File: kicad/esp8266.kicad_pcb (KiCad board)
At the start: 2 copper layers, 100 x 100 mm, 43 parts, among them J1 BATT, J2 Conn_Coaxial_Power, J3 CONN FT232RL, J4 RJ12, J5 RJ12, J6 Onewire, J7 Onewire, J8 Conn_01x01_Male, Q1 BSP75, Q2 BSP75, Q3 BSP75, Q4 BSP75, SW1 RESET, SW2 PROG, U1 ESP-12E, U2 MCP73831-2, U3 MCP1703A-3302_SOT23, U4 MS5637, U5 MCP1703A-5002_SOT23, U6 Si7020-A20, U7 DS18B20

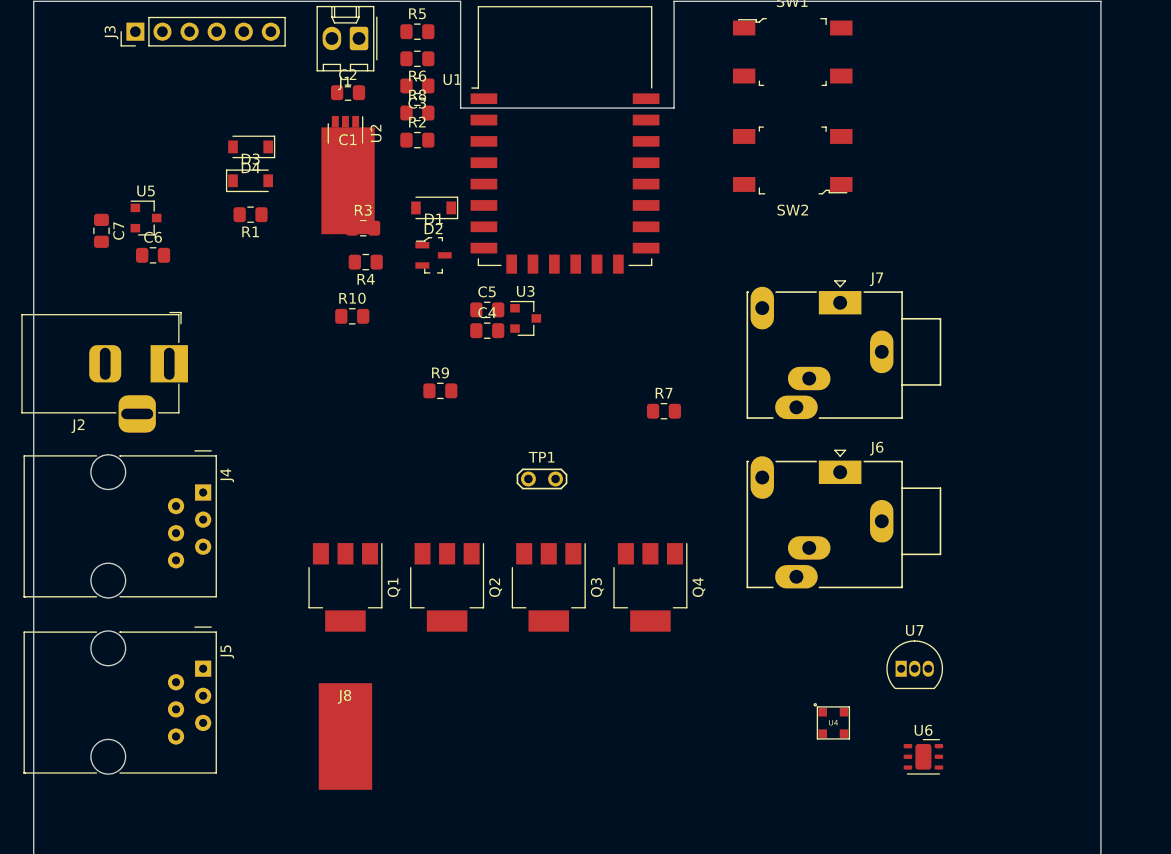
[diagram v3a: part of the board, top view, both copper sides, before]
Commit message: add test points in kicad
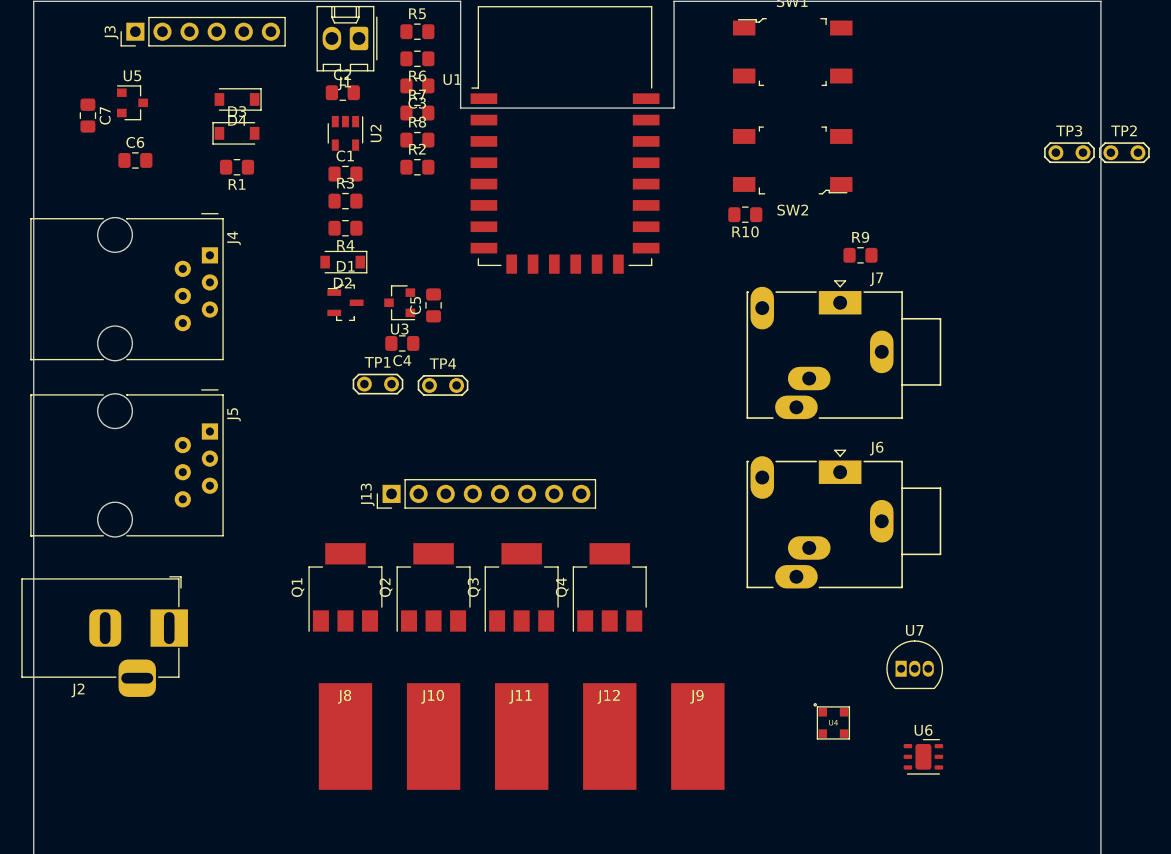
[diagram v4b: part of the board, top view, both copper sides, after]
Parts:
- added J10: Green, Connector_Wire:SolderWirePad_1x01_SMD_5x10mm, F.Cu at (115.5, 130.9)
- added J11: Blue, Connector_Wire:SolderWirePad_1x01_SMD_5x10mm, F.Cu at (123.7, 130.9)
- added J12: White, Connector_Wire:SolderWirePad_1x01_SMD_5x10mm, F.Cu at (132.0, 130.9)
- added J13: Conn_01x08_Female, Connector_PinHeader_2.54mm:PinHeader_1x08_P2.54mm_Vertical, F.Cu at (111.5, 108.2)
- added J9: Pad, Connector_Wire:SolderWirePad_1x01_SMD_5x10mm, F.Cu at (140.2, 130.9)
- added TP2: TestPoint_2Pole, TestPoint:TestPoint_2Pads_Pitch2.54mm_Drill0.8mm, F.Cu at (178.9, 76.2)
- added TP3: TestPoint_2Pole, TestPoint:TestPoint_2Pads_Pitch2.54mm_Drill0.8mm, F.Cu at (173.8, 76.2)
- added TP4: TestPoint_2Pole, TestPoint:TestPoint_2Pads_Pitch2.54mm_Drill0.8mm, F.Cu at (115.1, 98.0)
- C1: footprint Connector_Wire:SolderWirePad_1x01_SMD_5x10mm -> Capacitor_SMD:C_0805_2012Metric_Pad1.15x1.40mm_HandSolder
- J8: value Conn_01x01_Male -> Red
- moved R9 41.4 mm to (155.5, 85.8)
- moved R10 38.0 mm to (144.7, 82.0), turned to 180 degrees
- moved R7 36.3 mm to (114.0, 72.5)
- moved J2 24.8 mm to (90.7, 120.7)
- moved J4 22.2 mm to (94.5, 85.8)
- moved J5 22.2 mm to (94.5, 102.3)
- moved TP1 17.8 mm to (109.0, 97.9)
- moved U3 11.9 mm to (112.3, 90.2), turned to 180 degrees
- moved C7 10.9 mm to (83.1, 72.7)
- moved U5 10.9 mm to (87.3, 71.5)
- moved D2 9.91 mm to (107.0, 86.4)
- moved D1 9.38 mm to (107.2, 90.2)
- moved C6 9.04 mm to (87.5, 76.9)
- moved C4 8.05 mm to (112.5, 94.1), turned to 180 degrees
- moved C5 5.05 mm to (115.5, 90.5), turned to 90 degrees
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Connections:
- net /VBAT renamed +BATT
- Q2 pad 1: Net-(Q2-Pad1) -> /IO13
- Q2 pad 3: Net-(Q2-Pad3) -> GND
- Q3 pad 1: Net-(Q3-Pad1) -> /IO14
- Q3 pad 3: Net-(Q3-Pad3) -> GND
- Q4 pad 1: Net-(Q4-Pad1) -> /IO15
- Q4 pad 3: Net-(Q4-Pad3) -> GND
- U4 pad 1: Net-(U4-Pad1) -> +3V3
- U4 pad 2: Net-(U4-Pad2) -> /SDA
- U4 pad 3: Net-(U4-Pad3) -> /SCL
- U4 pad 4: Net-(U4-Pad4) -> GND
- U6 pad 1: Net-(U6-Pad1) -> /SDA
- U6 pad 2: Net-(U6-Pad2) -> GND
- U6 pad 5: Net-(U6-Pad5) -> +3V3
- U6 pad 6: Net-(U6-Pad6) -> /SCL

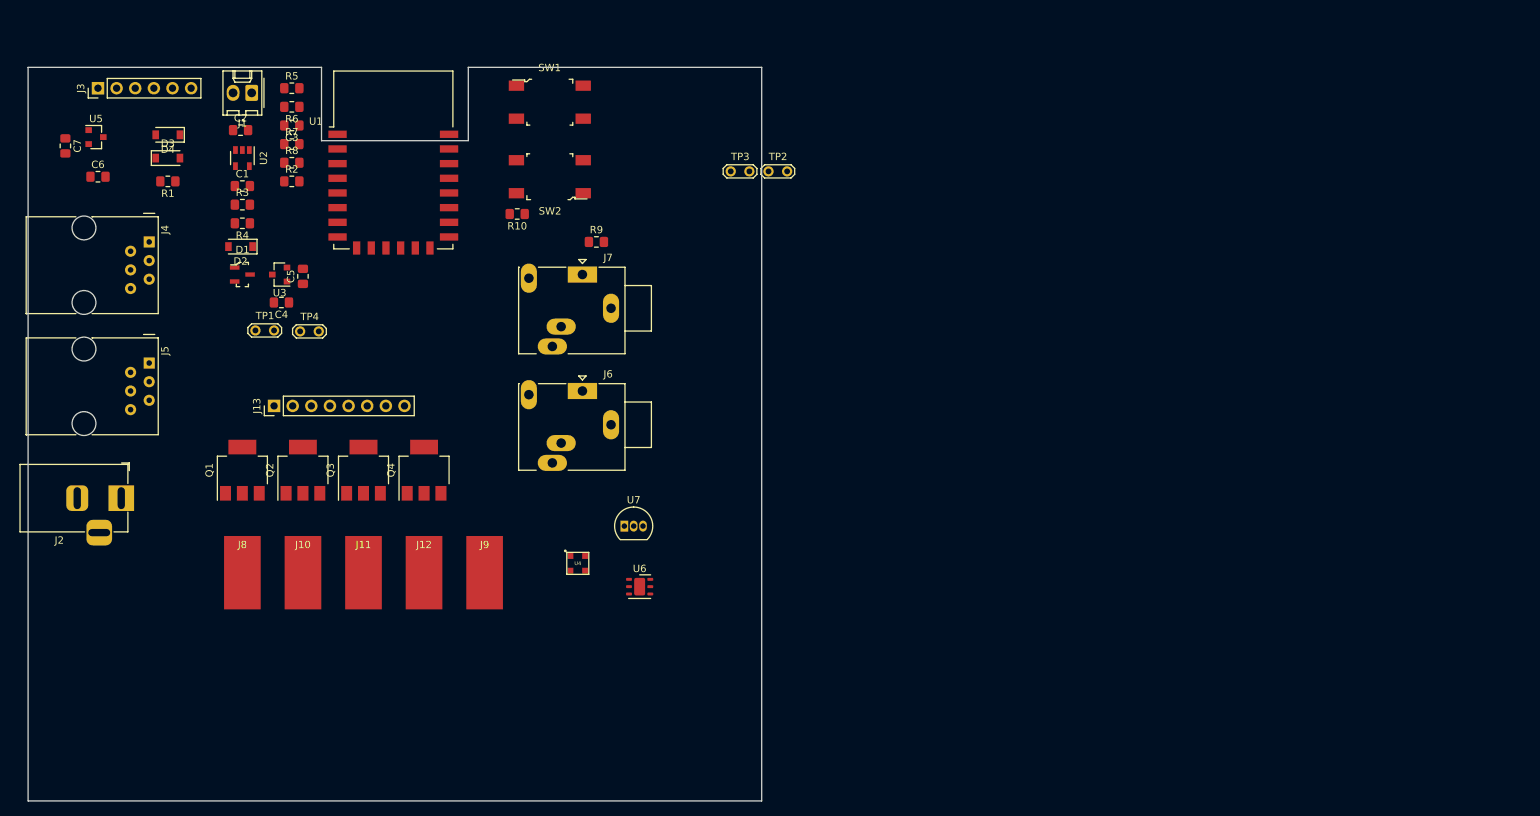
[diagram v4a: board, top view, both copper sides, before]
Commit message: add more test points
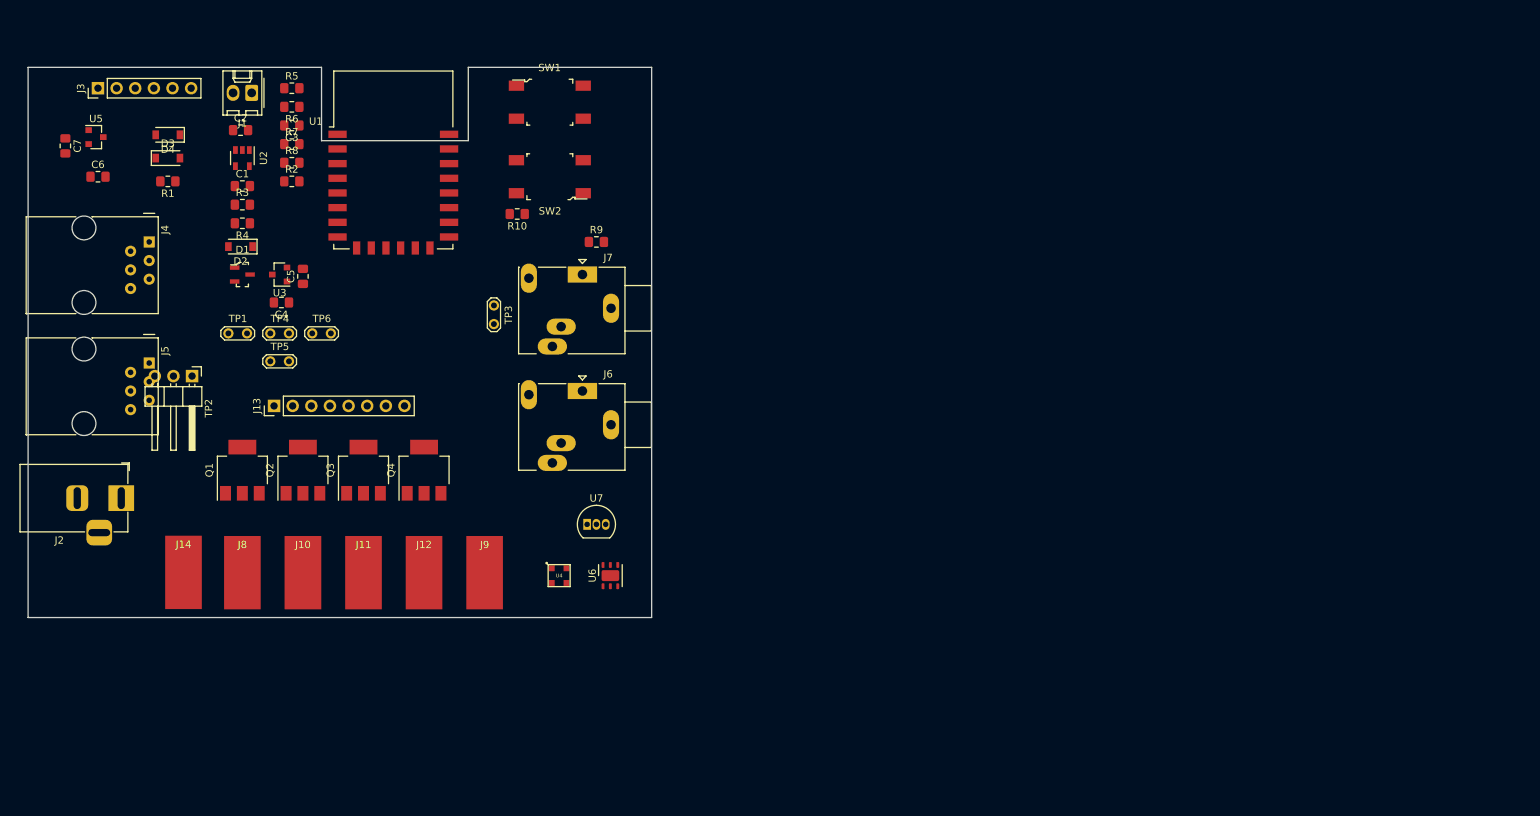
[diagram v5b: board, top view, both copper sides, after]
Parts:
- added J14: +12V, Connector_Wire:SolderWirePad_1x01_SMD_5x10mm, F.Cu at (99.2, 130.8)
- added TP5: V_OUT, TestPoint:TestPoint_2Pads_Pitch2.54mm_Drill0.8mm, F.Cu at (111.0, 102.1)
- added TP6: 3.3V, TestPoint:TestPoint_2Pads_Pitch2.54mm_Drill0.8mm, F.Cu at (116.7, 98.3)
- J13: value Conn_01x08_Female -> IO_RGBW
- J2: value Conn_Coaxial_Power -> 5 / 12V
- J4, J5: value RJ12 -> RJ12-I2C
- TP1: value TestPoint_2Pole -> 5V
- TP2: value TestPoint_2Pole -> Test_i2C; footprint TestPoint:TestPoint_2Pads_Pitch2.54mm_Drill0.8mm -> Connector_PinHeader_2.54mm:PinHeader_1x03_P2.54mm_Horizontal
- TP3: value TestPoint_2Pole -> OneWire
- TP4: value TestPoint_2Pole -> V_BAT
- U3: value MCP1703A-3302_SOT23 -> MCP1703-33
- U5: value MCP1703A-5002_SOT23 -> MCP1703-50
- moved TP2 83.4 mm to (100.4, 104.1), turned to 270 degrees
- moved TP3 37.1 mm to (141.5, 94.5), turned to 270 degrees
- moved U7 5.09 mm to (154.2, 124.3)
- moved U6 4.26 mm to (157.4, 131.3), turned to 90 degrees
- moved TP4 4.07 mm to (111.0, 98.3)
- moved TP1 3.70 mm to (105.3, 98.3)
- moved U4 3.04 mm to (150.4, 131.3)
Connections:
- C3 pad 1: /ADC -> Net-(C3-Pad1)
- C6 pad 2: /MCP1703-50/VDD -> +12V
- C7 pad 2: /MCP1703-50/3.3V -> /MCP1703-50/5.0V
- D3 pad 2: Net-(D3-Pad2) -> /MCP1703-50/5.0V
- J4 pad 1: Net-(J4-Pad1) -> +12V
- J4 pad 2: Net-(J4-Pad2) -> /SCL
- J4 pad 3: Net-(J4-Pad3) -> /SDA
- J4 pad 4: Net-(J4-Pad4) -> GND
- J4 pad 5: Net-(J4-Pad5) -> +BATT
- J4 pad 6: Net-(J4-Pad6) -> GND
- J5 pad 1: Net-(J5-Pad1) -> +12V
- J5 pad 2: Net-(J5-Pad2) -> /SCL
- J5 pad 3: Net-(J5-Pad3) -> /SDA
- J5 pad 4: Net-(J5-Pad4) -> GND
- J5 pad 5: Net-(J5-Pad5) -> +BATT
- J5 pad 6: Net-(J5-Pad6) -> GND
- R5 pad 2: /ADC -> Net-(C3-Pad1)
- R6 pad 1: /ADC -> Net-(C3-Pad1)
- TP1 pad 1: /MCP1703-33/VDD -> /MCP1703-50/5.0V
- TP4 pad 1: +3V3 -> +BATT
- U5 pad 2: /MCP1703-50/3.3V -> /MCP1703-50/5.0V
- U5 pad 3: /MCP1703-50/VDD -> +12V
- U7 pad 1: Net-(U7-Pad1) -> GND
- U7 pad 2: Net-(U7-Pad2) -> /IO2
- U7 pad 3: Net-(U7-Pad3) -> +3V3
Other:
- board size 100 x 100 mm -> 85 x 75 mm

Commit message: working on routing
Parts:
- TP2: footprint Connector_PinHeader_2.54mm:PinHeader_1x03_P2.54mm_Horizontal -> Connector_PinHeader_2.54mm:PinHeader_1x03_P2.54mm_Vertical
- moved TP1 38.5 mm to (81.8, 67.8), turned to 90 degrees
- moved R3 10.4 mm to (107.2, 70.3), turned to 180 degrees
- moved R10 9.53 mm to (154.2, 82.4)
- moved C7 6.96 mm to (88.8, 76.7), turned to 0 degrees
- moved TP5 6.87 mm to (105.3, 98.3)
- moved C6 5.32 mm to (85.0, 72.2), turned to 90 degrees
- moved TP3 3.18 mm to (138.3, 94.5)
- moved C2 2.32 mm to (107.2, 72.9)
- moved U6 2.01 mm to (159.3, 131.9)
- moved U2 1.91 mm to (107.2, 76.3)
- moved C1 1.90 mm to (107.2, 80.1)
- moved U5 1.76 mm to (88.7, 72.5), turned to 90 degrees
- moved TP2 1.48 mm to (101.6, 103.3), turned to 0 degrees
- moved R9 1.29 mm to (154.2, 85.6), turned to 180 degrees
- moved U4 0.90 mm to (151.0, 131.9)
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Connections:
- C3 pad 1: Net-(C3-Pad1) -> /ADC
- R5 pad 2: Net-(C3-Pad1) -> /ADC
- R6 pad 1: Net-(C3-Pad1) -> /ADC
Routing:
- net +12V: track 0.00 -> 136.2 mm
- net +BATT: track 0.00 -> 93.6 mm
- net /IO2: track 0.00 -> 77.2 mm
- net /IO13: track 0.00 -> 57.9 mm
- net GND: track 0.00 -> 54.8 mm, vias 0 -> 7
- net /IO12: track 0.00 -> 54.7 mm
- net +3V3: track 0.00 -> 54.4 mm
- net /IO14: track 0.00 -> 50.1 mm
- net /RST: track 0.00 -> 48.2 mm
- net /IO15: track 0.00 -> 43.3 mm
- net /MCP73831/V_STATUS: track 0.00 -> 29.9 mm
- net Net-(R10-Pad2): track 0.00 -> 26.7 mm
- net /MCP1703-50/5.0V: track 0.00 -> 23.6 mm
- net /MCP73831/VIN: track 0.00 -> 19.3 mm
- net /SCL: track 0.00 -> 12.6 mm
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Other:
- outline, holes or cut-outs redrawn
- net class Power added: clearance 0.4, trace_width 1, via_dia 1.4, via_drill 0.8

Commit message: working on routing
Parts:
- moved U6 3.61 mm to (155.8, 130.8), turned to 180 degrees
- moved U4 3.42 mm to (147.8, 130.7)
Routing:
- net /SCL: track 12.6 -> 256.3 mm, vias 0 -> 4
- net /SDA: track 7.50 -> 237.6 mm, vias 0 -> 4
- net /RX: track 0.00 -> 49.9 mm, vias 0 -> 2
- net /TX: track 0.00 -> 46.6 mm, vias 0 -> 1
- net +3V3: track 54.4 -> 93.1 mm
- net Net-(R10-Pad2): track 26.7 -> 39.7 mm
- net GND: track 54.8 -> 65.6 mm, vias 7 -> 11
- net /MCP1703-33/VDD: track 10.9 -> 19.9 mm
- net +BATT: track 93.6 -> 100.3 mm
- net /RST: track 48.2 -> 47.4 mm

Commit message: first pcb v1.0
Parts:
- added C8: 10uF, Capacitor_SMD:C_0805_2012Metric_Pad1.15x1.40mm_HandSolder, F.Cu at (158.0, 81.1)
- added C9: 10uF, Capacitor_SMD:C_0805_2012Metric_Pad1.15x1.40mm_HandSolder, F.Cu at (149.7, 124.3)
- added G***: LOGO, libs:hackuarium, F.Cu at (127.2, 96.9)
- added J15: hole, MountingHole:MountingHole_3.2mm_M3, F.Cu at (159.9, 65.2)
- added J16: hole, MountingHole:MountingHole_3.2mm_M3, F.Cu at (81.2, 65.2)
- added J17: hole, MountingHole:MountingHole_3.2mm_M3, F.Cu at (159.9, 133.8)
- added J18: hole, MountingHole:MountingHole_3.2mm_M3, F.Cu at (81.2, 133.8)
- added TP7: Test_UART, Connector_PinHeader_2.54mm:PinHeader_1x03_P2.54mm_Vertical, F.Cu at (90.1, 69.7)
- moved J1 20.6 mm to (102.1, 85.1), turned to 0 degrees
- moved D2 16.7 mm to (108.2, 69.8)
- moved D1 16.4 mm to (108.2, 73.9)
- moved TP1 15.9 mm to (93.2, 78.9)
- moved R3 14.1 mm to (96.5, 79.5)
- moved R2 13.4 mm to (102.6, 70.3)
- moved C1 13.4 mm to (108.2, 66.8)
- moved R4 12.4 mm to (96.5, 76.9), turned to 0 degrees
- moved U4 8.64 mm to (145.3, 122.4)
- moved C5 7.55 mm to (114.3, 83.0)
- moved R5 7.39 mm to (114.2, 72.2)
- moved U3 7.27 mm to (110.8, 83.1)
- moved TP4 6.84 mm to (105.2, 94.7)
- moved C2 6.83 mm to (102.6, 77.9), turned to 180 degrees
- moved C4 6.70 mm to (110.8, 87.6)
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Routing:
- net +3V3: track 93.1 -> 160.7 mm
- net /MCP73831/V_STATUS: track 29.9 -> 2.54 mm
- net GND: track 65.6 -> 91.0 mm, vias 11 -> 14
- net /TX: track 46.6 -> 62.5 mm
- net +BATT: track 100.3 -> 84.4 mm, vias 0 -> 2
- net /MCP73831/VIN: track 19.3 -> 30.5 mm
- net /RX: track 49.9 -> 60.4 mm
- net /MCP1703-50/5.0V: track 23.6 -> 13.7 mm
- net /MCP1703-33/VDD: track 19.9 -> 25.8 mm
- net /RST: track 47.4 -> 42.3 mm
- net /VCC_FTDI: track 7.51 -> 4.57 mm
- net Net-(R2-Pad1): track 4.84 -> 2.49 mm
- net +12V: track 136.2 -> 134.2 mm
- net Net-(R3-Pad1): track 9.09 -> 7.57 mm
- net /SDA: track 237.6 -> 238.7 mm
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- added copper zone on B.Cu, net GND
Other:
- net class Power removed
- board text added: "ESP-12e Playground 1.0"
